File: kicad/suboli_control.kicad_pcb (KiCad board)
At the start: 2 copper layers, 125 x 95 mm, 45 parts, among them J1 DC barrel jack panel header 5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, J2 3.5 mm TRS input panel header, J4 3.5 mm TRS headphone panel he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, J5 MA12070 module power, J6 MA12070 module audio in, SW1 DPST power switch panel header, U1 TLE2426ILP

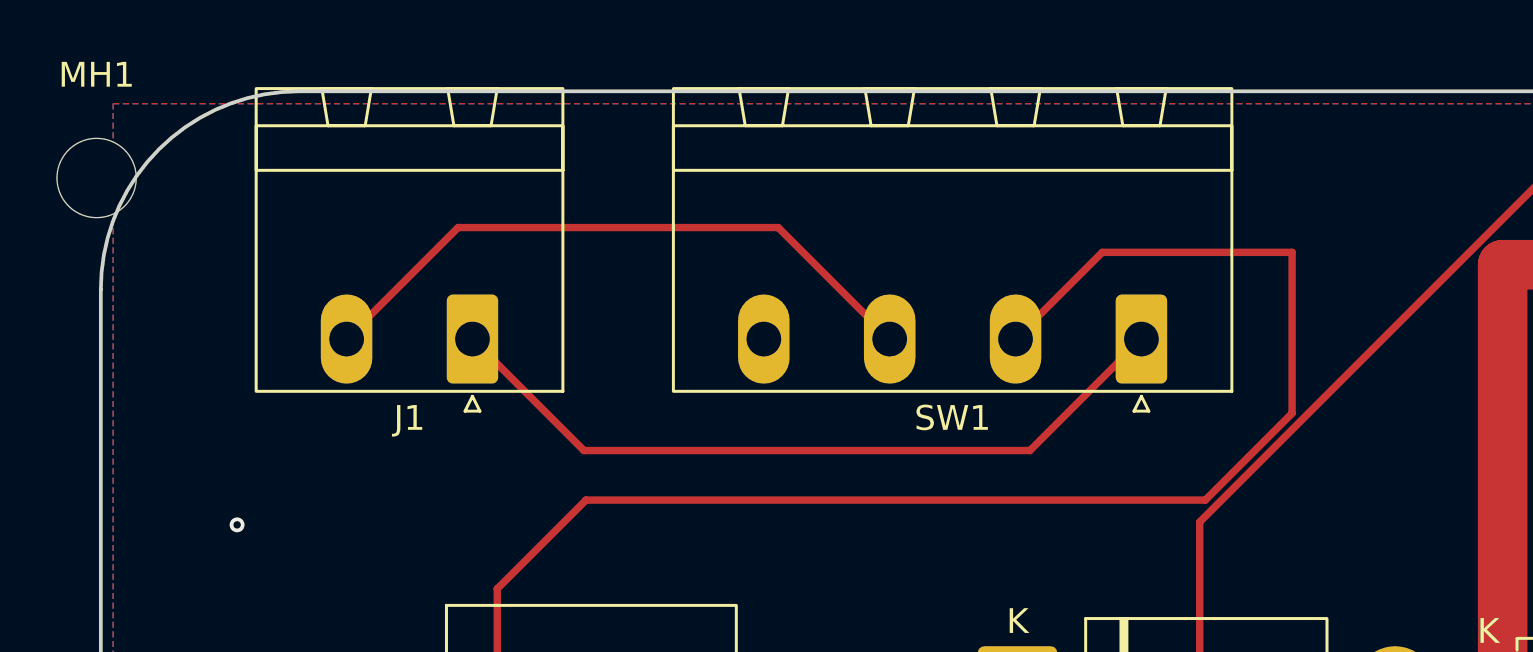
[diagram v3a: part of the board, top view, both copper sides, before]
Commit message: R23-wip: moved connectors + reconnected (16 DRC to resolve)
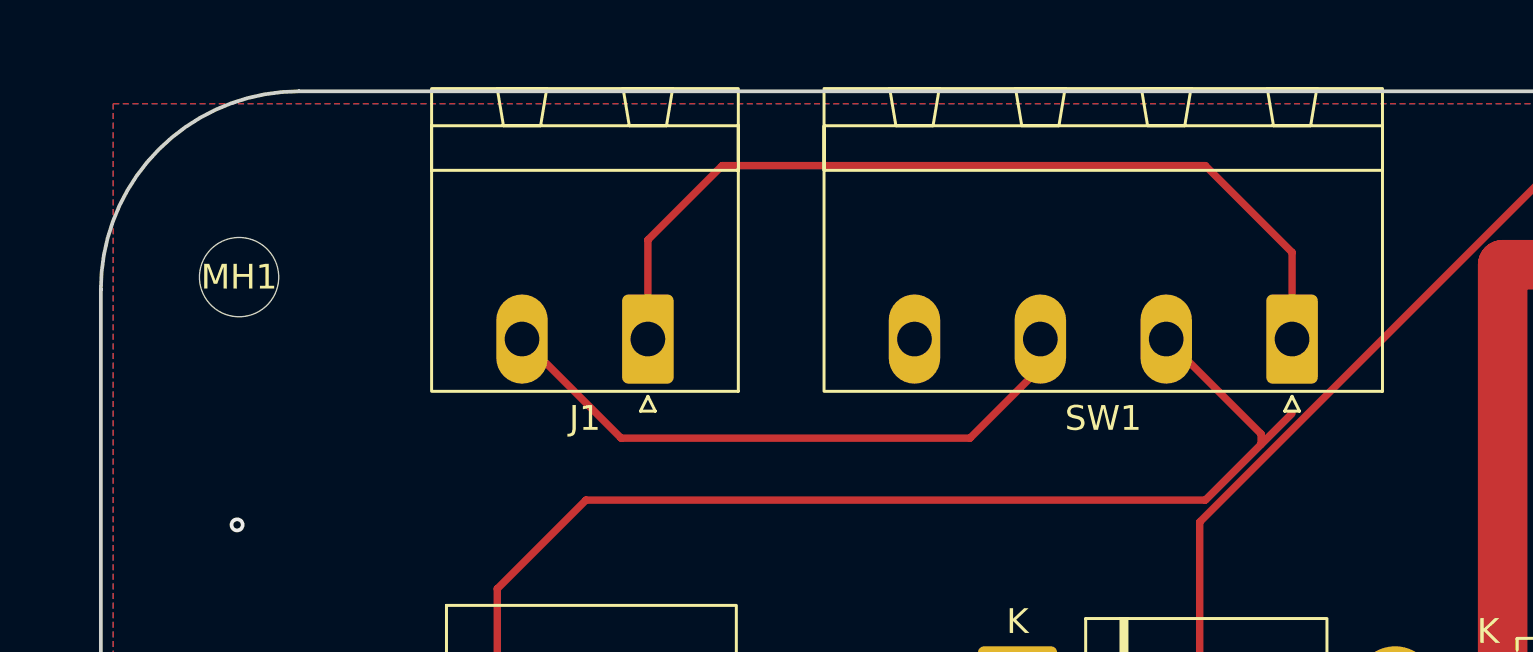
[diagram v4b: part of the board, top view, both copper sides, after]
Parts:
- moved J1 7.08 mm to (34.0, 22.0)
- moved MH1 7.00 mm to (17.5, 19.5)
- moved SW1 6.08 mm to (60.0, 22.0)
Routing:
- net /+19V_SW: track 58.0 -> 44.8 mm
- net /+19V_RAW: track 30.7 -> 36.2 mm
- net /GND_RAW: track 25.6 -> 24.9 mm
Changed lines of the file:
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@@
 	(footprint "MountingHole:MountingHole_3.2mm_M3"
 		(layer "F.Cu")
-		(at 11.75 15.5)
+		(at 17.5 19.5)
 		(descr "Mounting Hole 3.2mm, M3, no annular, generated by kicad-footprint-generator mountinghole.py")
 		(tags "mountinghole M3")
 		(property "Reference" "MH1"
-			(at 0 -4.15 0)
+			(at 0 0 0)
 			(layer "F.SilkS")
 			(effects
@@
 	(footprint "Connector_Phoenix_MSTB:PhoenixContact_MSTBA_2,5_4-G-5,08_1x04_P5.08mm_Horizontal"
 		(layer "F.Cu")
-		(at 53.92 22 180)
+		(at 60 22 180)
 		(descr "Generic Phoenix Contact connector footprint for: MSTBA_2,5/4-G-5,08; number of pins: 04; pin pitch: 5.08mm; Angled || order number: 1757268 12A || order number: 1923885 16A (HC)")
 		(tags "phoenix_contact connector MSTBA_01x04_G_5.08mm")
@@
 	(footprint "Connector_Phoenix_MSTB:PhoenixContact_MSTBA_2,5_2-G-5,08_1x02_P5.08mm_Horizontal"
 		(layer "F.Cu")
-		(at 26.92 22 180)
+		(at 34 22 180)
 		(descr "Generic Phoenix Contact connector footprint for: MSTBA_2,5/2-G-5,08; number of pins: 02; pin pitch: 5.08mm; Angled || order number: 1757242 12A || order number: 1923869 16A (HC)")
 		(tags "phoenix_contact connector MSTBA_01x02_G_5.08mm")
@@
 	)
 	(segment
-		(start 49.42 26.5)
-		(end 31.42 26.5)
+		(start 34 18)
+		(end 34 22)
 		(width 0.3)
 		(layer "F.Cu")
@@
 	)
 	(segment
-		(start 31.42 26.5)
-		(end 26.92 22)
+		(start 37 15)
+		(end 34 18)
 		(width 0.3)
 		(layer "F.Cu")
@@
 	)
 	(segment
-		(start 53.92 22)
-		(end 49.42 26.5)
+		(start 60 18.5)
+		(end 56.5 15)
 		(width 0.3)
 		(layer "F.Cu")
@@
 	)
 	(segment
-		(start 56.5 28.5)
-		(end 31.5 28.5)
+		(start 60 22)
+		(end 60 18.5)
+		(width 0.3)
+		(layer "F.Cu")
+		(net "/+19V_RAW")
+	)
+	(segment
+		(start 56.5 15)
+		(end 37 15)
+		(width 0.3)
+		(layer "F.Cu")
+		(net "/+19V_RAW")
+	)
+	(segment
+		(start 58.75 25.83)
+		(end 54.92 22)
 		(width 0.3)
 		(layer "F.Cu")
@@
 	)
 	(segment
-		(start 60 18.5)
-		(end 60 25)
+		(start 56.5 28.5)
+		(end 31.5 28.5)
 		(width 0.3)
 		(layer "F.Cu")
@@
 	)
 	(segment
-		(start 52.34 18.5)
-		(end 60 18.5)
+		(start 58.75 26.25)
+		(end 56.5 28.5)
 		(width 0.3)
 		(layer "F.Cu")
@@
 	(segment
 		(start 60 25)
-		(end 56.5 28.5)
+		(end 58.75 26.25)
 		(width 0.3)
 		(layer "F.Cu")
@@
 	)
 	(segment
-		(start 48.84 22)
-		(end 52.34 18.5)
+		(start 58.75 26.25)
+		(end 58.75 25.83)
 		(width 0.3)
 		(layer "F.Cu")
@@
 	)
 	(segment
-		(start 26.34 17.5)
-		(end 21.84 22)
+		(start 47 26)
+		(end 49.84 23.16)
+		(width 0.3)
+		(layer "F.Cu")
+		(net "/GND_RAW")
+	)
+	(segment
+		(start 32.92 26)
+		(end 47 26)
 		(width 0.3)
 		(layer "F.Cu")
@@
 	)
 	(segment
-		(start 39.26 17.5)
-		(end 26.34 17.5)
+		(start 49.84 23.16)
+		(end 49.84 22)
 		(width 0.3)
 		(layer "F.Cu")
@@
 	)
 	(segment
-		(start 43.76 22)
-		(end 39.26 17.5)
+		(start 28.92 22)
+		(end 32.92 26)
 		(width 0.3)
 		(layer "F.Cu")

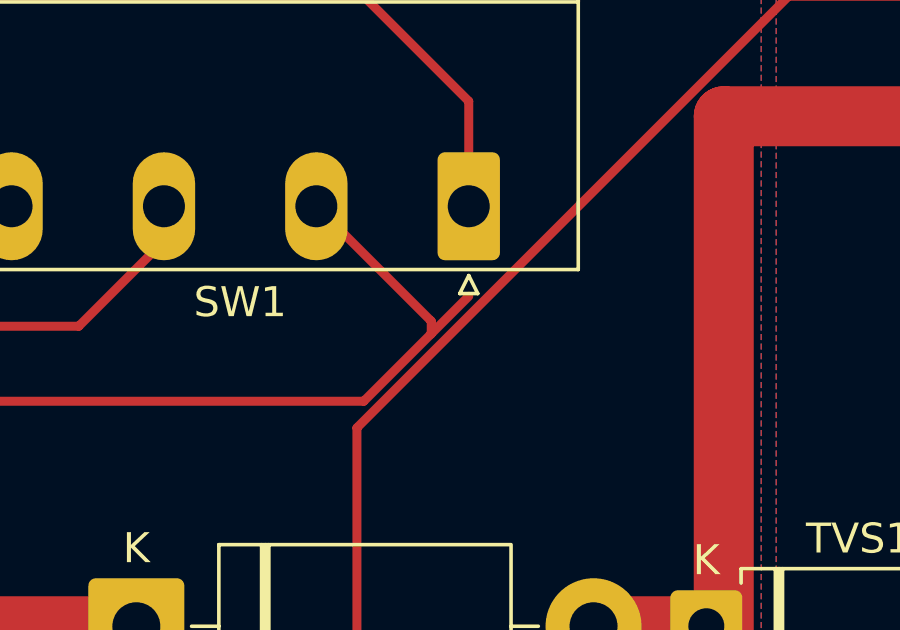
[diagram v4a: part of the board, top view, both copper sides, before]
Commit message: R23: resolve real DRC after connector moves
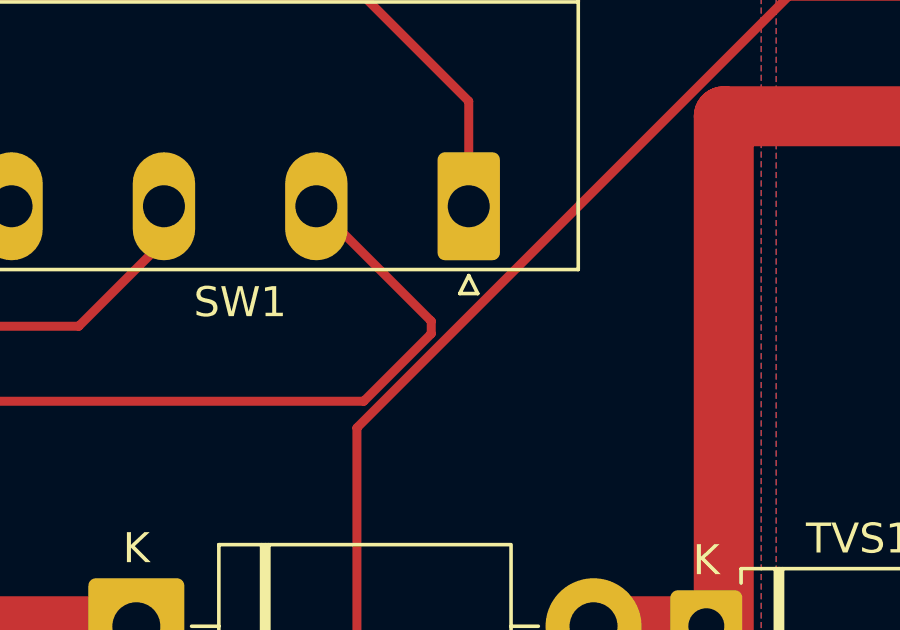
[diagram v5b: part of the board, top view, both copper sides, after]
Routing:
- net /+19V_SW: track 44.8 -> 43.0 mm
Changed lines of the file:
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@@
-	)
-	(segment
-		(start 60 25)
-		(end 58.75 26.25)
-		(width 0.3)
-		(layer "F.Cu")
-		(net "/+19V_SW")
 	)
 	(segment
